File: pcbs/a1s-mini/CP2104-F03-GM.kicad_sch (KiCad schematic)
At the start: 12 parts, among them U3 CP2102-GM

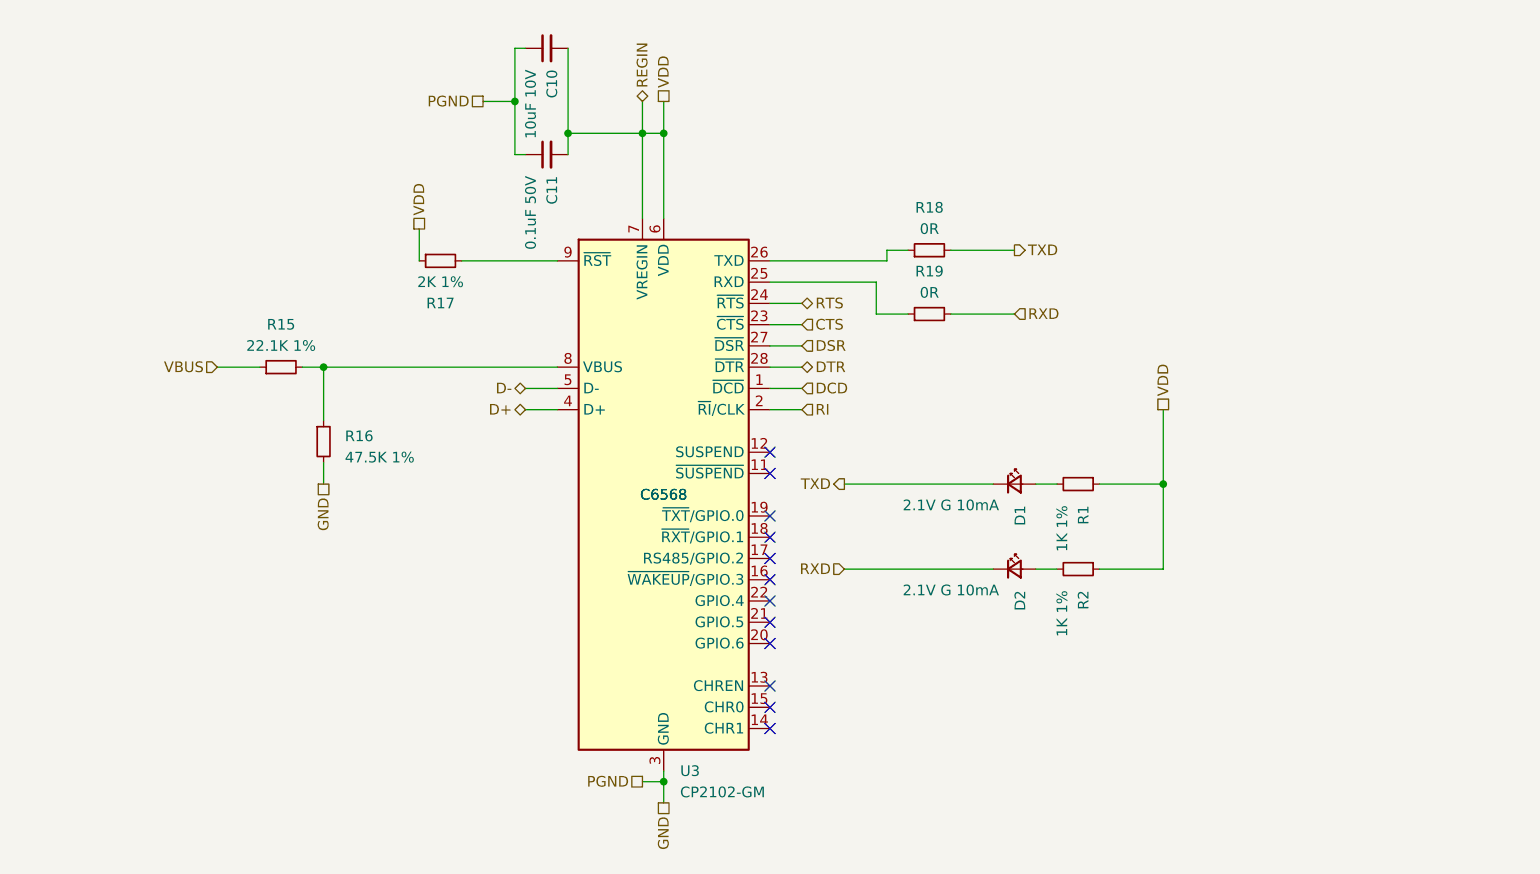
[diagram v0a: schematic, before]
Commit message: A1S updated to CP2104
Version numbers also updated
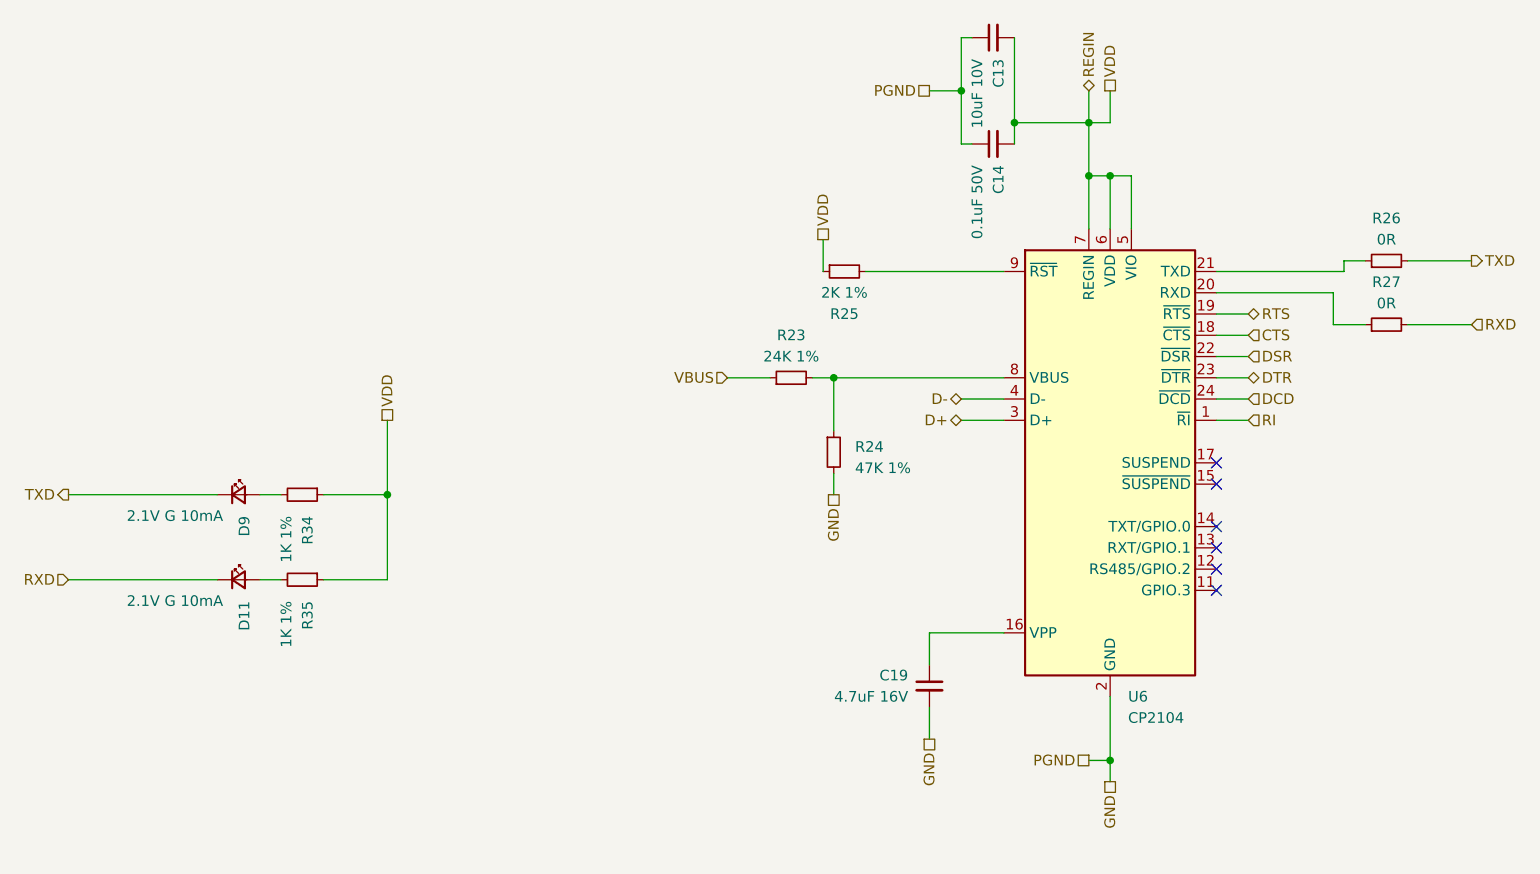
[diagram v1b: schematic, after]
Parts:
- removed U3: CP2102-GM, Package_DFN_QFN:QFN-28-1EP_5x5mm_P0.5mm_EP3.35x3.35mm, symbol Interface_USB:CP2102N-Axx-xQFN28
- added C19: 4.7uF 16V, Capacitor_SMD:C_0603_1608Metric, symbol Device:C_Small
- added U6: CP2104, Package_DFN_QFN:QFN-24-1EP_4x4mm_P0.5mm_EP2.6x2.6mm_ThermalVias, symbol Interface_USB:CP2104
- R23: renamed from R15; value 22.1K 1% -> 24K 1%; LCSC C6397988 -> C137760; LCSC alt C2960862 -> C137760; Manufacturer_Name StackPole Electronics -> Yageo; Manufacturer_Part_Number RMCF0603FT22K1 -> RC0603FR-0724KL
- R24: renamed from R16; value 47.5K 1% -> 47K 1%; LCSC C403243 -> C278626; LCSC alt C2933225 -> C278626; Manufacturer_Part_Number ERJ-3EKF4752V -> ERJ-3EKF4702V
- renumbered C10 to C13, C11 to C14, D2 to D11, D1 to D9, R17 to R25, R18 to R26, R19 to R27, R1 to R34, R2 to R35
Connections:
- net CTS: now also U6.18 (~{CTS})
- net D+: now also U6.3 (D+)
- net D-: now also U6.4 (D-)
- net DCD: now also U6.24 (~{DCD})
- net DSR: now also U6.22 (~{DSR})
- net DTR: now also U6.23 (~{DTR})
- net GND: now also C19.2, U6.2 (GND), U6.25 (GND)
- net REGIN: now also U6.5 (VIO), U6.6 (VDD), U6.7 (REGIN)
- net RI: now also U6.1 (~{RI})
- net RTS: now also U6.19 (~{RTS})
- net at R27.1: now also U6.20 (RXD)
- net at R23.2, R24.1: now also U6.8 (VBUS)
- net at R26.1: now also U6.21 (TXD)
- net at R25.2: now also U6.9 (~{RST})
- new net: C19.1, U6.16 (VPP)
- no-connect marks 12 -> 6
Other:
- title: CP2102 GM -> CP2104 interface
- moved on the sheet: C13, C14, D11, D9, R23, R24, R25, R26, R27, R34, R35
